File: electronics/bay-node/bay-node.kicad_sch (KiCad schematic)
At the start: 0 parts

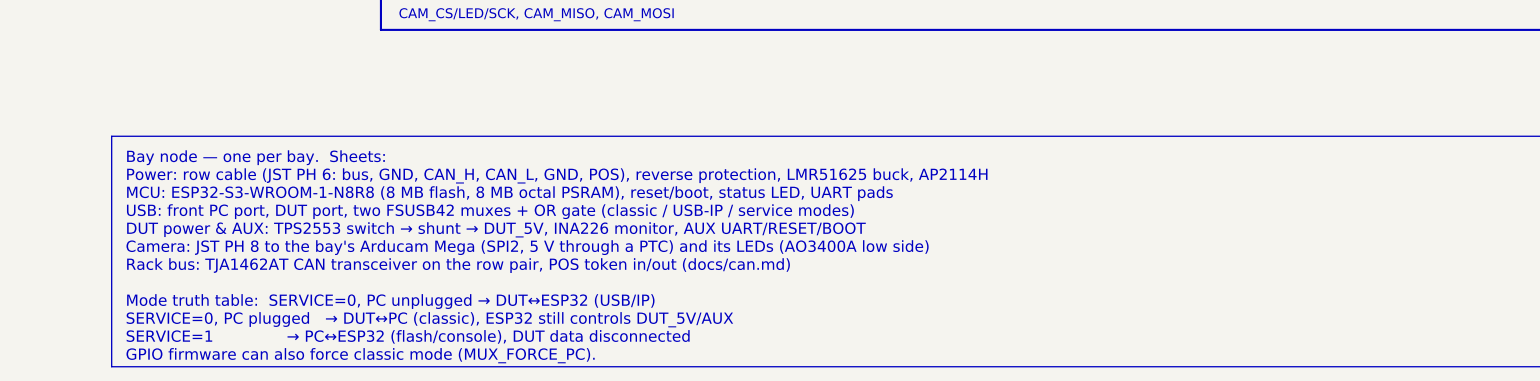
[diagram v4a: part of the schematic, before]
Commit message: Datasheet audit F1-F6: the pod's AP2114H, STB 5.1k, PC_DET hysteresis, the camera ESD's 100 nF, the eFuse step
The user approved the audit's fixes for the node, the hub and the pod
("Go pour 1"); docs/datasheet-audit.md marks F1-F6 applied.

* F1, camera pod: U1 AMS1117-3.3 -> AP2114H-3.3TRG1 (C150716, catalog
  ldo_1a, the node's U2).
  - The AMS1117 is specified stable only with 22 uF tantalum; the
    AP2114H is stable with the ceramic C2.
  - Same SOT-223 pinout, copper (the +3V3 pour and island round the
    tab stay) and 180 deg CPL correction.
  - One more extended type on the pod's Economic order: +$3.09 and
    $0.05 of parts (JLC_SINCE_QUOTE).
* F2, power hub: R214 (TJA1462 STB pull-down) 10k -> 5.1k (C23186,
  already on the board). With IO9 floating, STB's internal pull-up
  (20 kOhm minimum) left it at up to 1.10 V, over VIL 0.99 V.
* F3, bay node: R42 150k from MUX_SEL back to PC_DET, beside U7 (C22807,
  on the board since S1).
  - The laptop's VBUS rises at ~50 us/V through R11/R12, where the
    LVC1G32 wants <= 10 ns/V and warns of oscillation.
  - This gives ~0.14 V of hysteresis.
* F4, bay node: C28 100 nF (C14663) on U12/U13's VBUS pins (+3V3), above
  U12 by its pin 5. Between the two ICs their courtyards leave no room.
* F5, node and hub: firmware.md's first-flash procedure gains the
  irreversible DIS_USB_OTG_DOWNLOAD_MODE eFuse step. In USB-OTG
  download boot the ROM drives IO40 high: the node's DUT_FLT_N, the
  hub's PD_SCL. Nothing is burnt.
* F6, notes, hub:
  - the IMON filter is 0.9 ms, not 47 us: the pin is a current source;
  - the buck stops at ~3.8 V (internal UVLO);
  - SHDN turns on at >= 1 V;
  - the soft start stays under the limit only typically;
  - the CH224A note follows CH224 V2.1: the source PDOs are listed for
    both parts and readable under 100 W, which is still to check with
    ours (review R3); single-byte transfers; no "same die".
* F6, notes, node: TPS2553D; the LDO's 1.94 V x 0.4 A ~ 0.8 W; L1's
  7.5 A guarante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
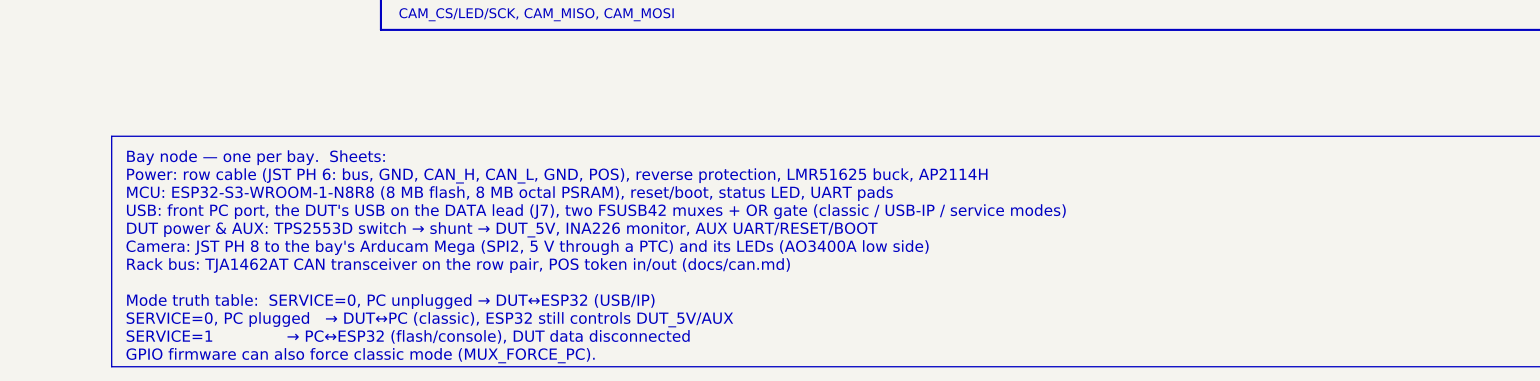
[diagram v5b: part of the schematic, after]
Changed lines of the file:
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@@
 		(comment 1 "ESP32-S3 USB/IP host for one bay of the hw-testing-rack shelf")
 		(comment 2 "Generated from electronics/bay-node/design.py — edit the Python, then regenerate")
-		(comment 3 "Row bus 20–28 V + CAN + POS in/out · 5 V/1.4 A switched DUT port · USB 2.0 muxes · INA226 · AUX")
+		(comment 3 "Row bus 20–28 V + CAN + POS in/out · 5 V/1.4 A switched DUT power on the DATA lead · USB 2.0 muxes · INA226 · AUX")
 	)
 	(sheet
@@
 		)
 	)
-	(text_box "Bay node — one per bay.  Sheets:\n  Power: row cable (JST PH 6: bus, GND, CAN_H, CAN_L, GND, POS), reverse protection, LMR51625 buck, AP2114H\n  MCU: ESP32-S3-WROOM-1-N8R8 (8 MB flash, 8 MB octal PSRAM), reset/boot, status LED, UART pads\n  USB: front PC port, DUT port, two FSUSB42 muxes + OR gate (classic / USB-IP / service modes)\n  DUT power & AUX: TPS2553 switch → shunt → DUT_5V, INA226 monitor, AUX UART/RESET/BOOT\n  Camera: JST PH 8 to the bay's Arducam Mega (SPI2, 5 V through a PTC) and its LEDs (AO3400A low side)\n  Rack bus: TJA1462AT CAN transceiver on the row pair, POS token in/out (docs/can.md)\n\nMode truth table:  SERVICE=0, PC unplugged → DUT↔ESP32 (USB/IP)\n                   SERVICE=0, PC plugged   → DUT↔PC (classic), ESP32 still controls DUT_5V/AUX\n                   SERVICE=1               → PC↔ESP32 (flash/console), DUT data disconnected\nGPIO firmware can also force classic mode (MUX_FORCE_PC)."
+	(text_box "Bay node — one per bay.  Sheets:\n  Power: row cable (JST PH 6: bus, GND, CAN_H, CAN_L, GND, POS), reverse protection, LMR51625 buck, AP2114H\n  MCU: ESP32-S3-WROOM-1-N8R8 (8 MB flash, 8 MB octal PSRAM), reset/boot, status LED, UART pads\n  USB: front PC port, the DUT's USB on the DATA lead (J7), two FSUSB42 muxes + OR gate (classic / USB-IP / service modes)\n  DUT power & AUX: TPS2553D switch → shunt → DUT_5V, INA226 monitor, AUX UART/RESET/BOOT\n  Camera: JST PH 8 to the bay's Arducam Mega (SPI2, 5 V through a PTC) and its LEDs (AO3400A low side)\n  Rack bus: TJA1462AT CAN transceiver on the row pair, POS token in/out (docs/can.md)\n\nMode truth table:  SERVICE=0, PC unplugged → DUT↔ESP32 (USB/IP)\n                   SERVICE=0, PC plugged   → DUT↔PC (classic), ESP32 still controls DUT_5V/AUX\n                   SERVICE=1               → PC↔ESP32 (flash/console), DUT data disconnected\nGPIO firmware can also force classic mode (MUX_FORCE_PC)."
 		(exclude_from_sim no)
 		(at 30 179.07 0)

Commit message: Bay node: 15 more labelled bottom test pads (BN-2)
The kicad-happy review's BN-2, against Eve's rule: no pad on the camera
SPI, CAN TXD/RXD, POS_IN/POS_OUT, or the DUT's UART1 and RESET/BOOT, and
all three GND pads in the x 43-46 column.  TP18-TP32 are bare pads on
B.Cu, named on B.SilkS and kept out of the BOM and the CPL.  The
signals are 1.0 mm and each group's GND 1.5 mm:
- the camera SPI by R31-R34, on the lead side of the 33 ohm resistors:
  SCK, MOSI, MISO, CS, GND;
- by U11: CAN TXD, RXD, POS IN, GND;
- by the AUX column: AUX TX, AUX RX, RST, BOOT, POS OUT, GND.

Each pad sits where its net already runs, so no routing moves:
- 8 on a new via drawn on one of the net's F.Cu tracks (the three GNDs
  in the pours);
- 7 on one of the net's B.Cu tracks.
None adds a via on In2's VRACK strip.  All pads are at least 2 mm
from any through-hole pad or hole and 2.6 mm from each other, and no
B.SilkS label overlaps another.  The schematic gets a test pad frame
on each of the Camera, Rack bus and DUT power & AUX sheets.

pcbgen.fanout_pads now leaves alone a pad that holds a drawn via of
its own net (a test pad on its own via).  Fanning it out was
redundant, and in an incremental route the fan-out vias landed on
other nets' tracks.  On the hub, the next regeneration drops TP38's
GND fan-out (1.1 mm and a via); nothing else changes there.

Every track and via is main's, plus one 3 mm CAN_TXD stub that the
router laid over the existing track to reach the new via.  ERC 0,
DRC 0, unconnected 0, parity 0.

Co-Authored-By: Claude Opus 5.5 <noreply@anthropic.com>
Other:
- note added: "AUX_BOOT_CTL, AUX_RST_CTL, AUX_RX/TX, DUT_EN, DUT_FLT_N, I2C_SCL/SDA, INA_ALERT_N, POS_OUT"
- note added: "POS_OUT"
- note removed: "AUX_BOOT_CTL, AUX_RST_CTL, AUX_RX/TX, DUT_EN, DUT_FLT_N, I2C_SCL/SDA, INA_ALERT_N"
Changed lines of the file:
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@@
 	(polyline
 		(pts
-			(xy 83.82 100.33)
-			(xy 83.82 133.35)
-			(xy 240.03 133.35)
-			(xy 240.03 100.33)
+			(xy 273.05 100.33)
+			(xy 273.05 133.35)
+			(xy 327.66 133.35)
+			(xy 327.66 100.33)
 		)
 		(stroke
@@
 		)
 	)
-	(text "AUX_BOOT_CTL, AUX_RST_CTL, AUX_RX/TX, DUT_EN, DUT_FLT_N, I2C_SCL/SDA, INA_ALERT_N"
+	(text "POS_OUT"
 		(exclude_from_sim no)
-		(at 86.36 132.08 0)
+		(at 275.59 132.08 0)
+		(effects
+			(font
+				(size 1.4 1.4)
+			)
+			(justify left bottom)
+		)
+	)
+	(polyline
+		(pts
+			(xy 83.82 100.33)
+			(xy 83.82 143.51)
+			(xy 247.65 143.51)
+			(xy 247.65 100.33)
+		)
+		(stroke
+			(width 0.3)
+			(type default)
+		)
+		(fill
+			(type none)
+		)
+	)
+	(text "AUX_BOOT_CTL, AUX_RST_CTL, AUX_RX/TX, DUT_EN, DUT_FLT_N, I2C_SCL/SDA, INA_ALERT_N, POS_OUT"
+		(exclude_from_sim no)
+		(at 86.36 142.24 0)
 		(effects
 			(font
@@
 		(pts
 			(xy 76.2 100.33)
-			(xy 76.2 143.51)
-			(xy 327.66 143.51)
-			(xy 327.66 100.33)
+			(xy 76.2 153.67)
+			(xy 335.28 153.67)
+			(xy 335.28 100.33)
 		)
 		(stroke
@@
 	(text "CAN_RXD/TXD, POS_IN/OUT"
 		(exclude_from_sim no)
-		(at 78.74 142.24 0)
+		(at 78.74 152.4 0)
 		(effects
 			(font
@@
 		(pts
 			(xy -2.54 100.33)
-			(xy -2.54 153.67)
-			(xy 335.28 153.67)
-			(xy 335.28 100.33)
+			(xy -2.54 163.83)
+			(xy 342.9 163.83)
+			(xy 342.9 100.33)
 		)
 		(stroke
@@
 	(text "CAN_H/L, POS_IN_CONN, POS_OUT_CONN"
 		(exclude_from_sim no)
-		(at 0 152.4 0)
+		(at 0 162.56 0)
 		(effects
 			(font
@@
 		(pts
 			(xy 68.58 100.33)
-			(xy 68.58 163.83)
-			(xy 421.64 163.83)
+			(xy 68.58 173.99)
+			(xy 421.64 173.99)
 			(xy 421.64 100.33)
 		)
@@
 	(text "CAM_CS/LED/SCK, CAM_MISO, CAM_MOSI"
 		(exclude_from_sim no)
-		(at 71.12 162.56 0)
+		(at 71.12 172.72 0)
 		(effects
 			(font
@@
 	(text_box "Bay node — one per bay.  Sheets:\n  Power: row cable (JST PH 6: bus, GND, CAN_H, CAN_L, GND, POS), reverse protection, LMR51625 buck, AP2114H\n  MCU: ESP32-S3-WROOM-1-N8R8 (8 MB flash, 8 MB octal PSRAM), reset/boot, status LED, UART pads\n  USB: front PC port, the DUT's USB on the DATA lead (J7), two FSUSB42 muxes + OR gate (classic / USB-IP / service modes)\n  DUT power & AUX: TPS2553D switch → shunt → DUT_5V, INA226 monitor, AUX UART/RESET/BOOT\n  Camera: JST PH 8 to the bay's Arducam Mega (SPI2, 5 V through a PTC) and its LEDs (AO3400A low side)\n  Rack bus: TJA1462AT CAN transceiver on the row pair, POS token in/out (docs/can.md)\n\nMode truth table:  SERVICE=0, PC unplugged → DUT↔ESP32 (USB/IP)\n                   SERVICE=0, PC plugged   → DUT↔PC (classic), ESP32 still controls DUT_5V/AUX\n                   SERVICE=1               → PC↔ESP32 (flash/console), DUT data disconnected\nGPIO firmware can also force classic mode (MUX_FORCE_PC)."
 		(exclude_from_sim no)
-		(at 30 179.07 0)
+		(at 30 189.23 0)
 		(size 360 33.02)
 		(margins 2 2 2 2)
